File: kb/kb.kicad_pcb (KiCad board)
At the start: 2 copper layers, 92 parts, among them SW1 SW_Push, SW10 SW_Push, SW11 SW_Push, SW12 SW_Push, SW13 SW_Push, SW14 SW_Push, SW15 SW_Push, SW16 SW_Push, SW17 SW_Push, SW18 SW_Push, SW19 SW_Push, SW2 SW_Push, SW20 SW_Push, SW21 SW_Push, SW22 SW_Push, SW23 SW_Push, SW24 SW_Push, SW25 SW_Push, SW26 SW_Push, SW27 SW_Push, SW28 SW_Push, SW29 SW_Push, SW3 SW_Push, SW30 SW_Push, SW31 SW_Push, SW32 SW_Push, SW33 SW_Push, SW34 SW_Push, SW35 SW_Push, SW36 SW_Push, SW37 SW_Push, SW38 SW_Push, SW39 SW_Push, SW4 SW_Push, SW40 SW_Push, SW41 SW_Push, SW42 SW_Push, SW43 SW_Push, SW44 SW_Push, SW45 SW_Push, SW46 SW_Push, SW5 SW_Push, SW6 SW_Push, SW7 SW_Push, SW8 SW_Push, SW9 SW_Push

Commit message: Improved routing
Edited schematic column layout,
Manually routed necessary keys on pcb
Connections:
- D45 pad 1: unconnected-(D45-K-Pad1) -> ROW3
- SW42 pad 1: COL5 -> COL6
- SW43 pad 1: COL6 -> COL8
- SW44 pad 1: COL7 -> COL9
- SW45 pad 1: COL8 -> COL10
- SW46 pad 1: COL9 -> COL11
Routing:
- net ROW0: track 442.9 -> 1328.7 mm
- net ROW1: track 419.1 -> 1304.9 mm
- net ROW2: track 423.9 -> 1309.7 mm
- net ROW3: track 404.8 -> 1143.0 mm
- net COL4: track 825.2 -> 1093.2 mm
- net COL8: track 549.2 -> 805.5 mm
- net Col0: track 765.7 -> 1021.9 mm
- net COL3: track 789.7 -> 1045.9 mm
- net COL9: track 549.2 -> 801.5 mm
- net COL10: track 65.0 -> 317.3 mm
- net COL11: track 21.0 -> 261.5 mm
- net COL6: track 549.2 -> 765.4 mm
- net COL1: track 549.2 -> 754.7 mm
- net COL2: track 549.2 -> 752.2 mm
- net COL7: track 549.2 -> 725.3 mm
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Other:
- board outline added: 256.6 x 81 mm

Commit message: 1.5u enter, fixed schematic
Fixed schematic & pcb for 1.5u enter layout
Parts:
- moved D36 231.8 mm to (271.8, 79.2)
- moved D24 217.5 mm to (267.0, 60.2)
- moved D46 38.4 mm to (271.8, 98.3)
- moved D39 33.3 mm to (83.7, 98.3)
- moved D42 33.3 mm to (178.9, 98.3)
- moved D40 31.0 mm to (117.0, 98.3)
- moved D25 31.0 mm to (50.3, 79.2)
- moved D41 31.0 mm to (148.0, 98.3)
- moved D43 21.4 mm to (212.2, 98.3)
- moved D37 21.4 mm to (40.8, 98.3)
- moved D38 21.4 mm to (62.2, 98.3)
- moved D28 19.1 mm to (119.4, 79.2)
- moved D30 19.1 mm to (157.5, 79.2)
- moved D31 19.1 mm to (176.5, 79.2)
- moved D33 19.1 mm to (214.6, 79.2)
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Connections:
- D24 pad 1: ROW2 -> ROW1
- D36 pad 1: ROW3 -> ROW2
- D46 pad 1: ROW1 -> ROW3
- SW24 pad 2: Net-(D46-A) -> Net-(D24-A)
- SW25 pad 2: Net-(D24-A) -> Net-(D25-A)
- SW26 pad 2: Net-(D25-A) -> Net-(D26-A)
- SW27 pad 2: Net-(D26-A) -> Net-(D27-A)
- SW28 pad 2: Net-(D27-A) -> Net-(D28-A)
- SW29 pad 2: Net-(D28-A) -> Net-(D29-A)
- SW30 pad 2: Net-(D29-A) -> Net-(D30-A)
- SW31 pad 2: Net-(D30-A) -> Net-(D31-A)
- SW32 pad 2: Net-(D31-A) -> Net-(D32-A)
- SW33 pad 2: Net-(D32-A) -> Net-(D33-A)
- SW34 pad 2: Net-(D33-A) -> Net-(D34-A)
- SW35 pad 2: Net-(D34-A) -> Net-(D35-A)
- SW36 pad 2: Net-(D35-A) -> Net-(D36-A)
- SW37 pad 2: Net-(D36-A) -> Net-(D37-A)
- SW38 pad 2: Net-(D37-A) -> Net-(D38-A)
- SW39 pad 2: Net-(D38-A) -> Net-(D39-A)
- SW40 pad 2: Net-(D39-A) -> Net-(D40-A)
- SW41 pad 2: Net-(D40-A) -> Net-(D41-A)
- SW42 pad 2: Net-(D41-A) -> Net-(D42-A)
- SW43 pad 2: Net-(D42-A) -> Net-(D43-A)
- SW44 pad 2: Net-(D43-A) -> Net-(D44-A)
- SW45 pad 2: Net-(D44-A) -> Net-(D45-A)
- SW46 pad 2: Net-(D45-A) -> Net-(D46-A)
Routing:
- net ROW0: track 1328.7 -> 221.5 mm
- net ROW2: track 1309.7 -> 221.5 mm
- net ROW1: track 1304.9 -> 221.5 mm
- net COL4: track 1093.2 -> 67.0 mm
- net COL3: track 1045.9 -> 64.1 mm
- net Col0: track 1021.9 -> 64.1 mm
- net ROW3: track 1143.0 -> 231.0 mm
- net COL8: track 805.5 -> 64.1 mm
- net COL9: track 801.5 -> 63.1 mm
- net COL6: track 765.4 -> 64.1 mm
- net COL1: track 754.7 -> 71.3 mm
- net COL2: track 752.2 -> 70.6 mm
- net COL7: track 725.3 -> 44.0 mm
- net COL5: track 725.3 -> 44.0 mm
- net COL10: track 317.3 -> 63.1 mm
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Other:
- board outline removed

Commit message: STM32 + Unified Daughterboard Implementation
Switched to run off STM32 and S1.1 Unified Daughterboard.
Wired rows and cols
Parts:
- added C10: 1uF, Capacitor_SMD:C_0805_2012Metric, F.Cu at (253.6, 185.4)
- added C11: 10nF, Capacitor_SMD:C_0805_2012Metric, F.Cu at (85.3, 162.1)
- added C12: 1uF, Capacitor_SMD:C_0805_2012Metric, F.Cu at (85.3, 166.1)
- added C13: 100nF, Capacitor_SMD:C_0805_2012Metric, F.Cu at (88.6, 166.1)
- added C14: 4.7uF, Capacitor_SMD:C_0805_2012Metric, F.Cu at (88.6, 170.1)
- added C2: 0.1uF, Capacitor_SMD:C_0805_2012Metric, F.Cu at (85.3, 170.1)
- added C3: 0.1uF, Capacitor_SMD:C_0805_2012Metric, F.Cu at (88.6, 173.9)
- added C4: 4.7uF, Capacitor_SMD:C_0805_2012Metric, F.Cu at (85.3, 174.2)
- added C5: .1uF, Capacitor_SMD:C_0805_2012Metric, F.Cu at (88.6, 162.2)
- added C8: 100nF, Capacitor_SMD:C_0805_2012Metric, F.Cu at (190.1, 194.7)
- added C9: 1uF, Capacitor_SMD:C_0805_2012Metric, F.Cu at (245.4, 185.4)
- added J1: Conn_01x04_MountingPin, Connector_Molex:Molex_Pico-EZmate_78171-0004_1x04-1MP_P1.20mm_Vertical, F.Cu at (118.9, 168.8)
- added R5: 10k, Resistor_SMD:R_0805_2012Metric, F.Cu at (147.8, 179.7)
- added SW48: SW_Push, Button_Switch_SMD:SW_SPST_SKQG_WithStem, F.Cu at (148.8, 185.8)
- added U1: USBLC6-2SC6, Package_TO_SOT_SMD:SOT-23-6, F.Cu at (197.5, 194.2)
- added U2: STM32G474CETx, Package_QFP:LQFP-48_7x7mm_P0.5mm, F.Cu at (188.2, 185.9)
- added U4: XC6206PxxxMR, Package_TO_SOT_SMD:SOT-23-3, F.Cu at (249.0, 185.3)
- moved D1 109.2 mm to (101.9, 133.2)
- moved D10 109.2 mm to (278.1, 133.2)
- moved D11 109.2 mm to (297.2, 133.2)
- moved D13 109.2 mm to (104.3, 152.2)
- moved D14 109.2 mm to (130.5, 152.2)
- moved D15 109.2 mm to (149.5, 152.2)
- moved D16 109.2 mm to (168.6, 152.2)
- moved D17 109.2 mm to (187.6, 152.2)
- moved D18 109.2 mm to (206.7, 152.2)
- moved D19 109.2 mm to (225.7, 152.2)
- moved D2 109.2 mm to (125.7, 133.2)
- moved D20 109.2 mm to (244.8, 152.2)
- moved D21 109.2 mm to (263.8, 152.2)
- moved D22 109.2 mm to (282.9, 152.2)
- moved D23 109.2 mm to (301.9, 152.2)
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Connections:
- net Col0 renamed COL0
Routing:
- net ROW0: track 221.5 -> 479.0 mm, vias 0 -> 1
- net COL10: track 63.1 -> 240.0 mm
- net COL9: track 63.1 -> 220.9 mm
- net COL0: track 64.1 -> 213.2 mm
- net COL8: track 64.1 -> 203.1 mm
- net COL1: track 71.3 -> 192.1 mm
- net COL7: track 44.0 -> 153.0 mm, vias 0 -> 2
- net COL2: track 70.6 -> 170.2 mm
- net COL6: track 64.1 -> 156.6 mm
- net COL4: track 67.0 -> 139.6 mm
- net COL5: track 44.0 -> 114.8 mm, vias 0 -> 2
- net COL3: track 64.1 -> 126.3 mm, vias 0 -> 2
- net COL11: track 60.1 -> 120.2 mm
- net +3V3: track 0.00 -> 56.9 mm, vias 0 -> 2
- net BOOT: track 0.00 -> 42.9 mm
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
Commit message: Wired PCB
Finished wiring PCB
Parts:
- moved J1 2.25 mm to (119.5, 166.6)
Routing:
- net +5V: track 0.00 -> 155.6 mm, vias 0 -> 4
- net COL11: track 120.2 -> 255.0 mm
- net D+: track 7.15 -> 105.3 mm, vias 0 -> 2
- net D-: track 8.49 -> 103.7 mm, vias 0 -> 2
- net +3V3: track 56.9 -> 129.6 mm, vias 2 -> 4
- net GND: track 26.4 -> 75.4 mm, vias 0 -> 7
- net ROW3: track 232.7 -> 234.9 mm
- added copper zone on F.Cu, net GND

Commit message: Fixed Board Side
Fixed Side of board
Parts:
- C10, C11, C12, C13, C14, C2, C3, C4, C5, C8, C9, J1, R5, SW48, U1, U2, U4: moved to B.Cu
- D1, D10, D11, D12, D13, D14, D15, D16, D17, D18, D19, D2, D20, D21, D22, D23, D24, D25, D26, D27, D28, D29, D3, D30, D31, D32, D33, D34, D35, D36, D37, D38, D39, D4, D40, D41, D42, D43, D44, D45, D46, D5, D6, D7, D8, D9: footprint Diode_SMD:D_0201_0603Metric -> Diode_SMD:D_0805_2012Metric
- moved SW48 195.5 mm to (272.4, 34.2), turned to 90 degrees
- moved C14 137.3 mm to (195.3, 83.7), turned to 45 degrees
- moved C11 135.4 mm to (197.1, 85.7), turned to 135 degrees
- moved C4 135.2 mm to (197.7, 99.1), turned to -45 degrees
- moved C12 134.7 mm to (200.5, 96.3), turned to 135 degrees
- moved C3 130.1 mm to (195.2, 99.3), turned to -45 degrees
- moved C5 129.8 mm to (193.3, 85.5), turned to 135 degrees
- moved C2 127.8 mm to (187.5, 93.2), turned to -135 degrees
- moved C13 122.4 mm to (185.7, 91.4), turned to -135 degrees
- moved C10 119.7 mm to (180.2, 90.9), turned to 45 degrees
- moved U4 113.5 mm to (182.7, 93.2), turned to -45 degrees
- moved D1 109.2 mm to (43.2, 41.1)
- moved D10 109.2 mm to (219.4, 41.1)
- moved D11 109.2 mm to (238.4, 41.1)
- moved D13 109.2 mm to (45.6, 60.2)
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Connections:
- U2 pad 10: COL2 -> COL9
- U2 pad 11: COL1 -> COL10
- U2 pad 12: COL0 -> COL11
- U2 pad 13: unconnected-(U2-PA5-Pad13) -> ROW3
- U2 pad 16: ROW3 -> unconnected-(U2-PB0-Pad16)
- U2 pad 27: COL11 -> unconnected-(U2-PB13-Pad27)
- U2 pad 28: COL10 -> unconnected-(U2-PB14-Pad28)
- U2 pad 29: COL9 -> unconnected-(U2-PB15-Pad29)
- U2 pad 30: COL8 -> unconnected-(U2-PA8-Pad30)
- U2 pad 31: COL6 -> unconnected-(U2-PA9-Pad31)
- U2 pad 32: COL4 -> unconnected-(U2-PA10-Pad32)
- U2 pad 33: COL7 -> unconnected-(U2-PA11-Pad33)
- U2 pad 34: COL5 -> unconnected-(U2-PA12-Pad34)
- U2 pad 37: unconnected-(U2-PA13-Pad37) -> COL0
- U2 pad 38: unconnected-(U2-PA14-Pad38) -> COL1
- U2 pad 39: unconnected-(U2-PA15-Pad39) -> COL2
- U2 pad 40: unconnected-(U2-PB3-Pad40) -> COL3
- U2 pad 41: unconnected-(U2-PB4-Pad41) -> COL4
- U2 pad 42: ROW0 -> COL5
- U2 pad 43: ROW1 -> COL6
- U2 pad 44: ROW2 -> ROW0
- U2 pad 45: unconnected-(U2-PB8-Pad45) -> ROW1
- U2 pad 46: unconnected-(U2-PB9-Pad46) -> ROW2
- U2 pad 8: unconnected-(U2-PA0-Pad8) -> COL7
- U2 pad 9: COL3 -> COL8
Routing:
- net ROW0: track 479.0 -> 280.6 mm, vias 1 -> 2
- net COL8: track 203.4 -> 72.2 mm, vias 0 -> 1
- net COL10: track 240.0 -> 109.3 mm, vias 0 -> 1
- net COL9: track 220.9 -> 90.8 mm, vias 0 -> 1
- net COL11: track 255.0 -> 125.3 mm, vias 0 -> 1
- net +5V: track 155.6 -> 48.0 mm
- net BOOT: track 42.9 -> 132.5 mm
- net COL7: track 153.0 -> 67.8 mm, vias 2 -> 1
- net COL6: track 156.6 -> 91.7 mm, vias 0 -> 1
- net D+: track 105.3 -> 40.8 mm
- net D-: track 103.7 -> 43.9 mm, vias 2 -> 0
- net +3V3: track 129.6 -> 160.8 mm, vias 4 -> 2
- net COL3: track 126.3 -> 147.9 mm, vias 2 -> 1
- net ROW3: track 234.9 -> 256.1 mm, vias 1 -> 0
- net GND: track 75.4 -> 96.4 mm, vias 7 -> 2
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- added copper zone on B.Cu, net GND

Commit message: Fixed Decoupling
Fix decoupling cap placement + amounts, added ground layer, thickened vdd traces, completed routing
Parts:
- removed C14: 4.7uF, Capacitor_SMD:C_0805_2012Metric
- added C1: 1uF, Capacitor_SMD:C_0805_2012Metric, B.Cu at (203.3, 98.0)
- C2, C3: value 0.1uF -> 100nF
- C5: value .1uF -> 100nF
- moved C3 13.0 mm to (197.4, 86.5), turned to 135 degrees
- moved C11 12.8 mm to (198.0, 98.5), turned to -45 degrees
- moved C13 11.5 mm to (194.2, 99.2)
- moved C4 10.5 mm to (187.8, 95.5)
- moved C2 10.4 mm to (194.4, 85.5), turned to 45 degrees
- moved C5 8.91 mm to (187.5, 92.2)
- moved C12 5.32 mm to (197.1, 100.3), turned to -45 degrees
- moved R5 1.88 mm to (199.6, 86.0)
- moved C8 0.98 mm to (200.1, 97.6)
- moved C10 0.56 mm to (180.8, 90.9)
- moved U4 0.56 mm to (183.2, 93.2)
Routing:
- net GND: track 96.4 -> 51.1 mm, vias 2 -> 5
- net +3V3: track 160.8 -> 179.9 mm, vias 2 -> 4
- net Net-(U2-VREF+): track 2.23 -> 6.61 mm
- net BOOT: track 132.5 -> 130.2 mm
- net D+: track 40.8 -> 43.0 mm
- net D-: track 43.9 -> 46.0 mm
- net +5V: track 48.0 -> 47.8 mm, vias 4 -> 5

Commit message: Improved Ground Net
Rewired some components, fixed ground layer, seperated VSSA from VSS
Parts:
- moved R5 71.2 mm to (270.8, 83.8)
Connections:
- C11 pad 2: GND -> (no net)
- C12 pad 2: GND -> (no net)
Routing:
- net +3V3: track 179.9 -> 182.9 mm
- net BOOT: track 130.2 -> 131.8 mm
- net GND: track 51.1 -> 50.4 mm, vias 5 -> 6

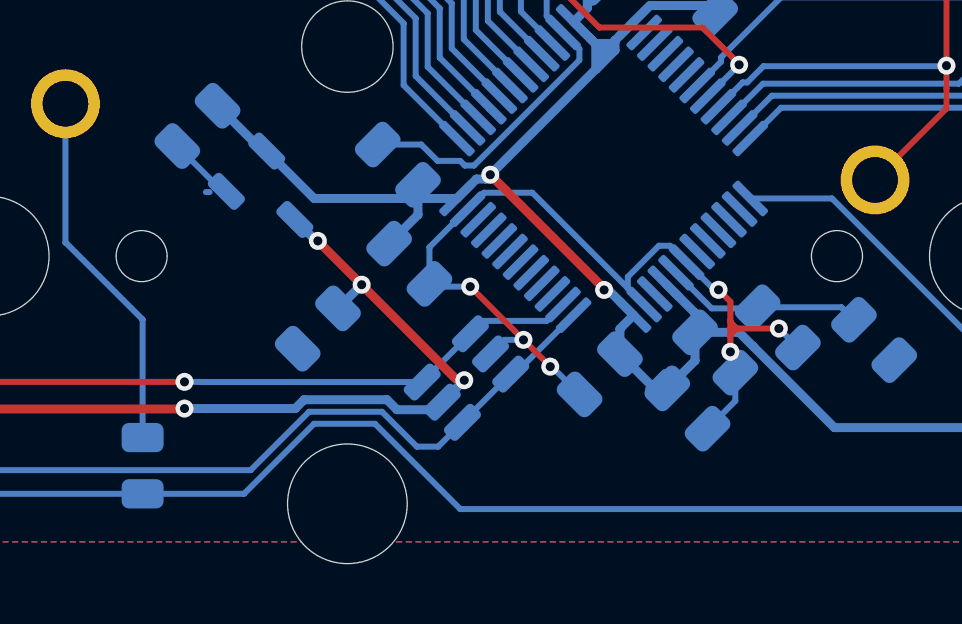
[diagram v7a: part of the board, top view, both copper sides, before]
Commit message: Fixed usb IO pins
Moved USB IO pins to 33/34 (PA11/PA12) where they belong
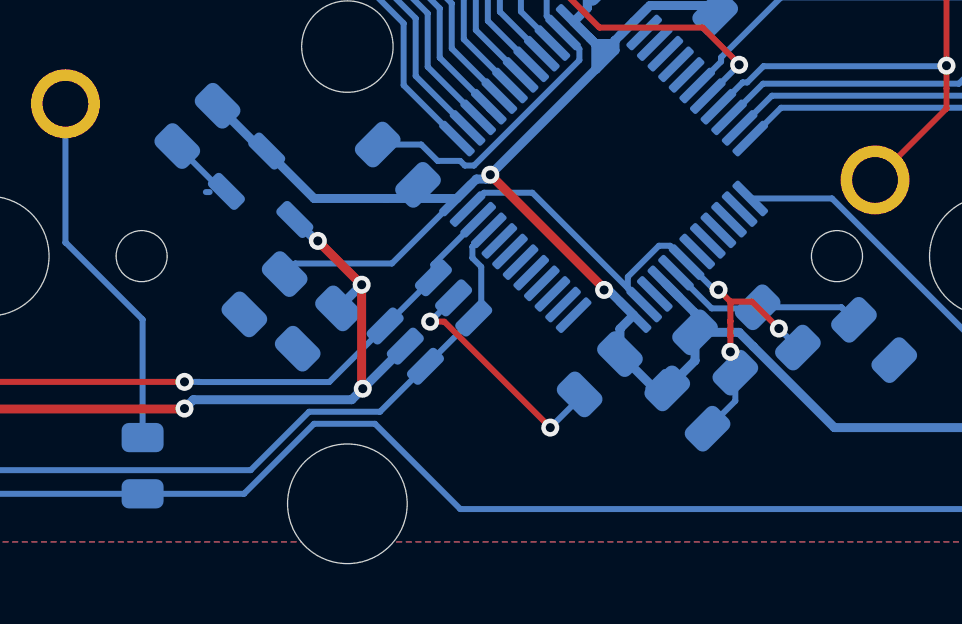
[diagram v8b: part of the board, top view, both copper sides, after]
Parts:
- moved C4 4.93 mm to (183.0, 96.5), turned to -135 degrees
- moved U1 2.24 mm to (188.5, 97.4)
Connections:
- U2 pad 25: D- -> unconnected-(U2-PB11-Pad25)
- U2 pad 26: D+ -> unconnected-(U2-PB12-Pad26)
- U2 pad 33: unconnected-(U2-PA11-Pad33) -> D-
- U2 pad 34: unconnected-(U2-PA12-Pad34) -> D+
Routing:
- net +3V3: track 182.9 -> 187.4 mm
- net +5V: track 47.8 -> 44.7 mm
- net GND: track 50.4 -> 47.4 mm, vias 6 -> 5
- net D+: track 43.0 -> 41.6 mm
- net D-: track 46.0 -> 45.2 mm
